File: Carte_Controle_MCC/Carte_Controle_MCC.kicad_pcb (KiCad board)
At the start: 2 copper layers, 35 parts, among them J1 USB_C_Receptacle_USB2.0_16P, J2 Conn_ST_STDC14, J3 Conn_01x02_XT60, J4 Conn_01x04_moteur, U1 USBLC6-2SC6, U2 STM32G431CBUx

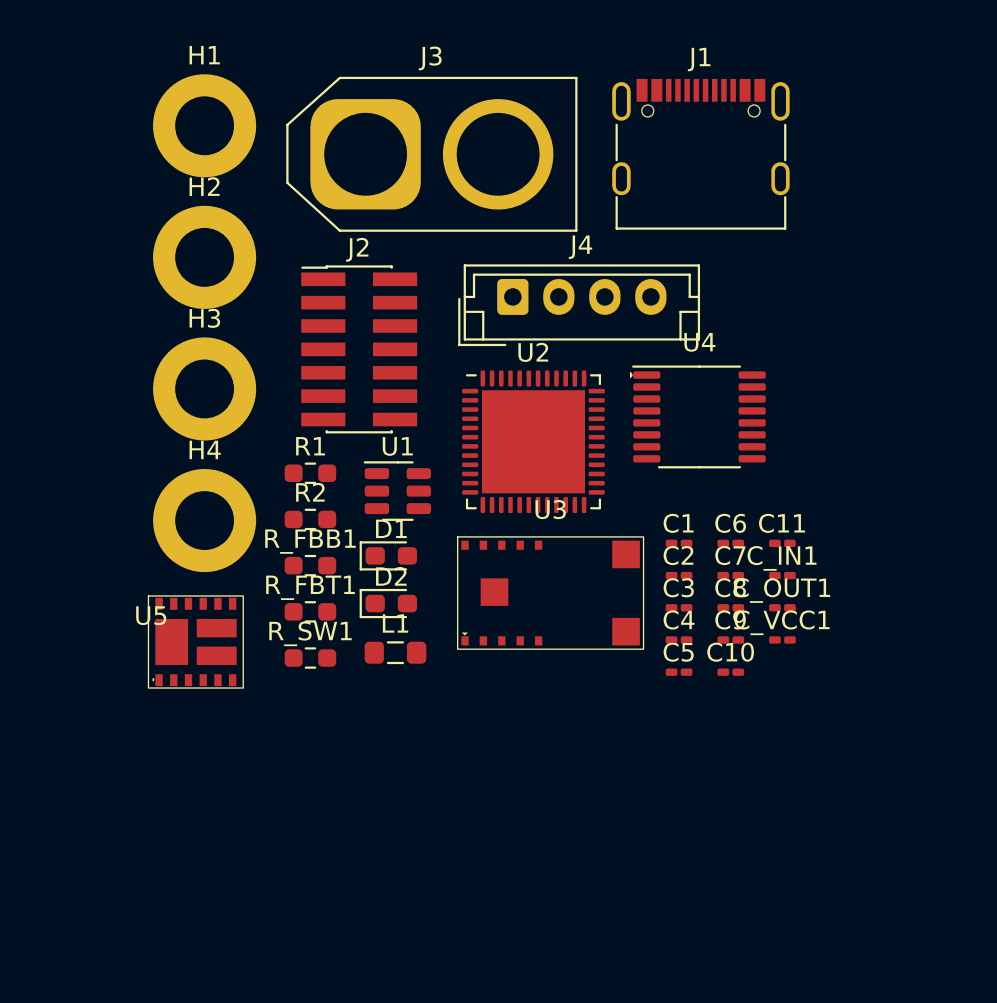
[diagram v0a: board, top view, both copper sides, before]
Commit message: routing of the PCB
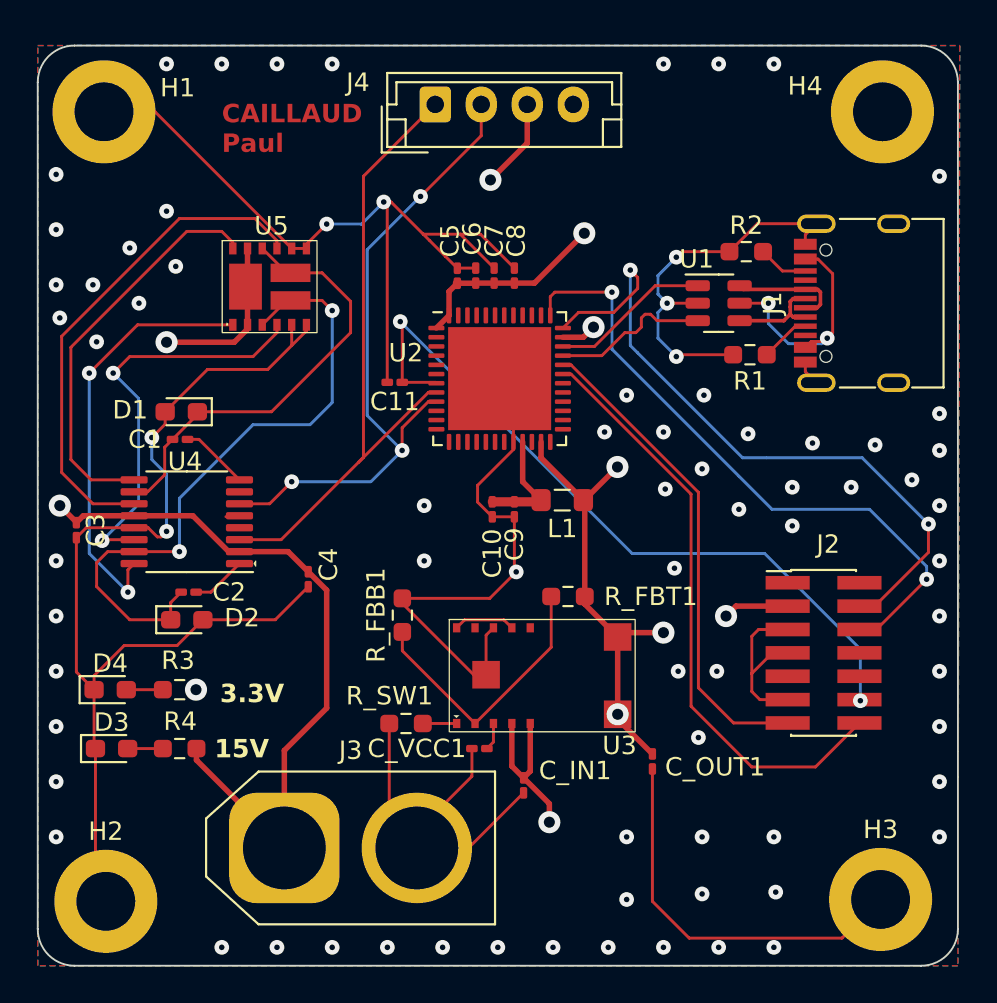
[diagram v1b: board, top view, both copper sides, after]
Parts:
- added D3: LED_Small, LED_SMD:LED_0603_1608Metric_Pad1.05x0.95mm_HandSolder, F.Cu at (114.0, 108.2)
- added D4: LED_Small, LED_SMD:LED_0603_1608Metric_Pad1.05x0.95mm_HandSolder, F.Cu at (113.9, 105.0)
- added R3: 820, Resistor_SMD:R_0603_1608Metric_Pad0.98x0.95mm_HandSolder, F.Cu at (117.7, 105.0)
- added R4: 5.6k, Resistor_SMD:R_0603_1608Metric_Pad0.98x0.95mm_HandSolder, F.Cu at (117.7, 108.2)
- moved H3 46.0 mm to (155.8, 116.4)
- moved H4 43.0 mm to (155.9, 73.6)
- moved J3 37.9 mm to (123.4, 113.6)
- moved H2 35.4 mm to (113.7, 116.5)
- moved C3 33.0 mm to (112.1, 96.3), turned to -90 degrees
- moved J2 30.1 mm to (152.7, 103.0)
- moved U4 28.4 mm to (118.1, 95.9), turned to 180 degrees
- moved R2 27.8 mm to (148.5, 81.2)
- moved C1 27.7 mm to (117.7, 91.4), turned to 180 degrees
- moved C2 26.7 mm to (118.2, 99.7)
- moved R1 24.7 mm to (148.7, 86.8), turned to 180 degrees
- moved C5 24.7 mm to (132.8, 82.5), turned to 90 degrees
- moved C11 22.8 mm to (129.4, 88.3), turned to 180 degrees
- moved C8 21.5 mm to (135.9, 82.5), turned to 90 degrees
- moved C7 20.8 mm to (134.8, 82.5), turned to 90 degrees
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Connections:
- J1 pad A1: ISO_GND -> GND
- J1 pad A12: ISO_GND -> GND
- J1 pad B1: ISO_GND -> GND
- J1 pad B12: ISO_GND -> GND
- J1 pad S1: ISO_GND -> GND
- R1 pad 2: ISO_GND -> GND
- R2 pad 1: ISO_GND -> GND
- U1 pad 2: ISO_GND -> GND
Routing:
- net GND: track 0.00 -> 209.6 mm, vias 0 -> 78
- net +15V: track 0.00 -> 63.1 mm, vias 0 -> 4
- net +3.3V: track 0.00 -> 41.1 mm, vias 0 -> 7
- net NRST: track 0.00 -> 40.5 mm, vias 0 -> 2
- net SYS_SWDIO: track 0.00 -> 36.9 mm, vias 0 -> 2
- net TIM2_CH2_PWM: track 0.00 -> 35.9 mm, vias 0 -> 3
- net S1/D2_INPUT: track 0.00 -> 35.5 mm, vias 0 -> 2
- net TIM2_CH1_PWM: track 0.00 -> 35.2 mm
- net SYS_SWCLK: track 0.00 -> 35.0 mm, vias 0 -> 2
- net USART_Tx: track 0.00 -> 32.7 mm
- net G3_INPUT: track 0.00 -> 27.3 mm
- net USART_Rx: track 0.00 -> 26.5 mm
- net S4/D3_INPUT: track 0.00 -> 24.0 mm
- net G1_INPUT: track 0.00 -> 23.3 mm, vias 0 -> 2
- net G2_INPUT: track 0.00 -> 22.5 mm, vias 0 -> 2
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- added copper zone on In2.Cu, net +15V
- added copper zone on In2.Cu, net +3.3V
- added copper zone on B.Cu, net GND
- added copper zone on F.Cu, net GND
- added copper zone on In1.Cu, net GND
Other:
- board outline added: 50 x 50 mm
- copper layers 2 -> 4
- board text added: "15V"
- board text added: "3.3V"
- board text added: "CAILLAUD Paul"

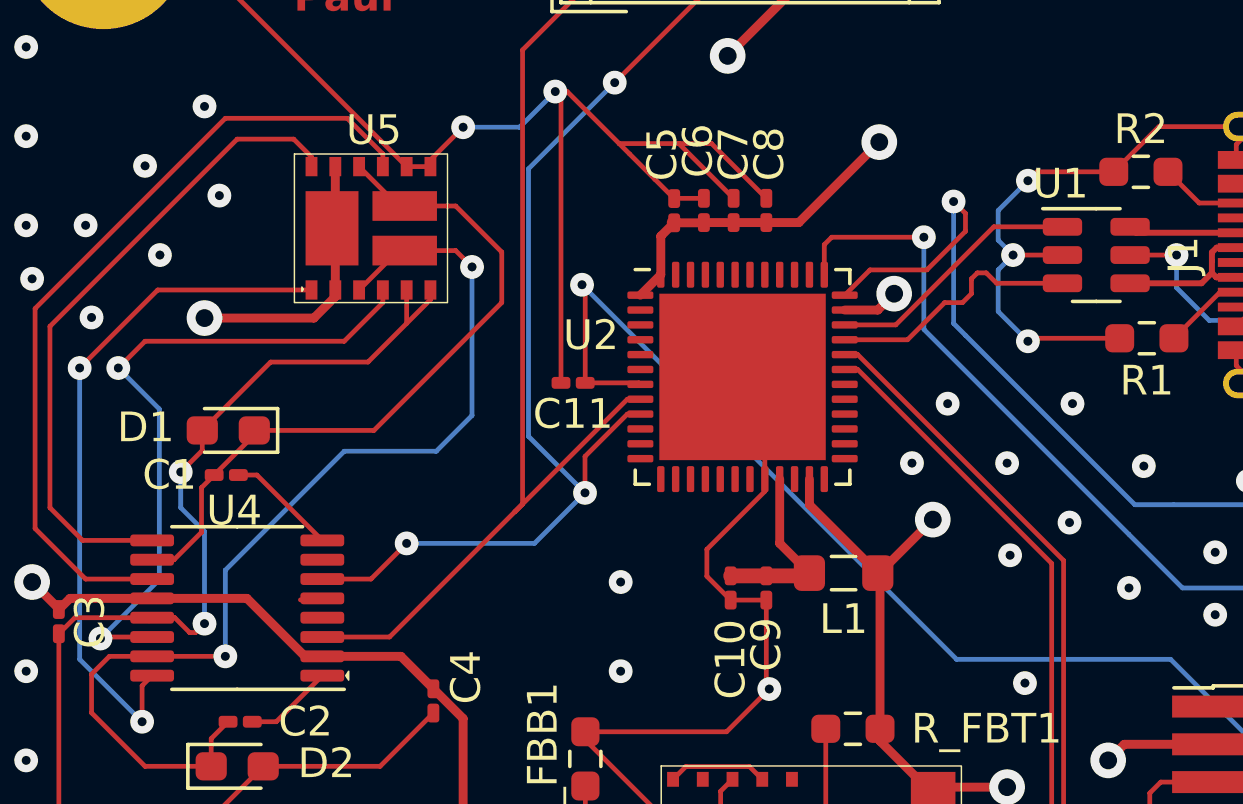
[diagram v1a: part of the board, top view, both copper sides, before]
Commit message: Suppression of unecessary ground tracks
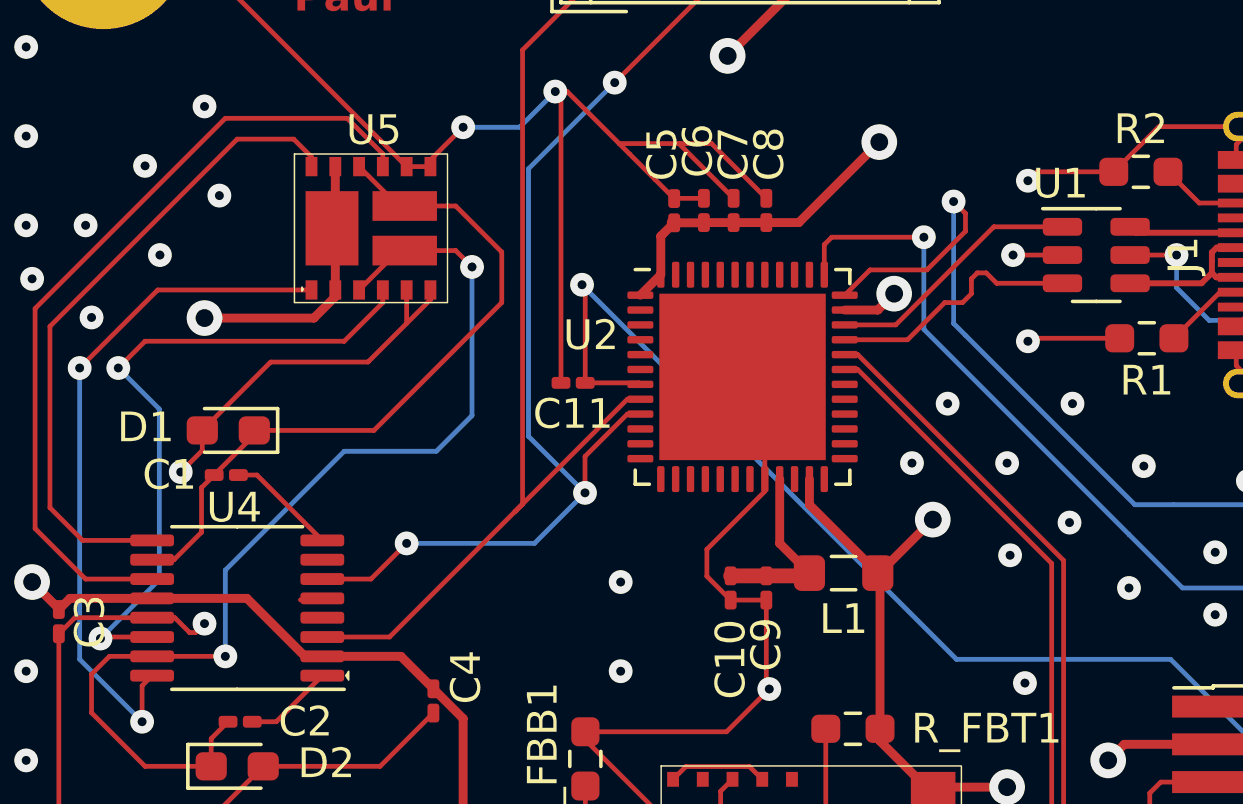
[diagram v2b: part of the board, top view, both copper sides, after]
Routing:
- net GND: track 209.6 -> 197.5 mm
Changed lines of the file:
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@@
     (property "Sheetname" "")
     (attr smd)
-    (fp_text reference "U4" (at 0.1 3.3 unlocked) (layer "F.SilkS")
+    (fp_text reference "U4" (at 0.1 3.4 unlocked) (layer "F.SilkS")
         (effects (font (size 1 1) (thickness 0.1)))
     )
@@
   (via (at 144.7 86.9) (size 0.8) (drill 0.3) (layers "F.Cu" "B.Cu") (net 6))
   (via (at 144 71) (size 0.8) (drill 0.3) (layers "F.Cu" "B.Cu") (free) (net 6))
-  (segment (start 143.7 84.5) (end 143.7 85.9) (width 0.16) (layer "B.Cu") (net 6))
-  (segment (start 117 93.3) (end 117 96.4) (width 0.16) (layer "B.Cu") (net 6))
   (segment (start 128.8 78.5) (end 127.6 79.7) (width 0.16) (layer "B.Cu") (net 6))
-  (segment (start 144.7 81.5) (end 143.7 82.5) (width 0.16) (layer "B.Cu") (net 6))
   (segment (start 127.6 79.7) (end 125.7 79.7) (width 0.16) (layer "B.Cu") (net 6))
-  (segment (start 116.2 91.3) (end 116.2 92.5) (width 0.16) (layer "B.Cu") (net 6))
-  (segment (start 116.8 93.1) (end 117 93.3) (width 0.16) (layer "B.Cu") (net 6))
-  (segment (start 143.7 85.9) (end 144.7 86.9) (width 0.16) (layer "B.Cu") (net 6))
-  (segment (start 143.7 83.5) (end 144.2 84) (width 0.16) (layer "B.Cu") (net 6))
-  (segment (start 116.2 92.5) (end 116.8 93.1) (width 0.16) (layer "B.Cu") (net 6))
-  (segment (start 143.7 82.5) (end 143.7 83.5) (width 0.16) (layer "B.Cu") (net 6))
-  (segment (start 144.2 84) (end 143.7 84.5) (width 0.16) (layer "B.Cu") (net 6))
   (segment (start 137 82.9) (end 139.7 80.2) (width 0.3) (layer "F.Cu") (net 7))
   (segment (start 132.35 84.6625) (end 132.35 83.365) (width 0.3) (layer "F.Cu") (net 7))
@@
   (segment (start 129.8125 101.8625) (end 129.8125 102.8875) (width 0.16) (layer "F.Cu") (net 29))
   (segment (start 130.925 106.8375) (end 132.7625 106.8375) (width 0.16) (layer "F.Cu") (net 30))
-  (segment (start 138.5375 86.35) (end 140.253087 86.35) (width 0.16) (layer "F.Cu") (net 31))
-  (segment (start 143.553087 83.05) (end 145.8625 83.05) (width 0.16) (layer "F.Cu") (net 31))
-  (segment (start 140.253087 86.35) (end 143.553087 83.05) (width 0.16) (layer "F.Cu") (net 31))
-  (segment (start 142.8 85.3) (end 142.8 84.8) (width 0.16) (layer "F.Cu") (net 32))
-  (segment (start 142.8 84.8) (end 143 84.6) (width 0.16) (layer "F.Cu") (net 32))
-  (segment (start 141.9 85.6) (end 142.5 85.6) (width 0.16) (layer "F.Cu") (net 32))
-  (segment (start 140.65 86.85) (end 141.9 85.6) (width 0.16) (layer "F.Cu") (net 32))
-  (segment (start 143 84.6) (end 143.3 84.6) (width 0.16) (layer "F.Cu") (net 32))
-  (segment (start 142.5 85.6) (end 142.8 85.3) (width 0.16) (layer "F.Cu") (net 32))
-  (segment (start 138.5375 86.85) (end 140.65 86.85) (width 0.16) (layer "F.Cu") (net 32))
-  (segment (start 143.65 84.95) (end 145.8625 84.95) (width 0.16) (layer "F.Cu") (net 32))
-  (segment (start 143.3 84.6) (end 143.65 84.95) (width 0.16) (layer "F.Cu") (net 32))
+  (segment (start 140.253087 86.35) (end 138.5375 86.35) (width 0.16) (layer "F.Cu") (net 31))
+  (segment (start 145.8625 83.05) (end 143.553087 83.05) (width 0.16) (layer "F.Cu") (net 31))
+  (segment (start 143.553087 83.05) (end 140.253087 86.35) (width 0.16) (layer "F.Cu") (net 31))
+  (segment (start 143 84.6) (end 142.8 84.8) (width 0.16) (layer "F.Cu") (net 32))
+  (segment (start 143.3 84.6) (end 143 84.6) (width 0.16) (layer "F.Cu") (net 32))
+  (segment (start 143.65 84.95) (end 143.3 84.6) (width 0.16) (layer "F.Cu") (net 32))
+  (segment (start 140.65 86.85) (end 138.5375 86.85) (width 0.16) (layer "F.Cu") (net 32))
+  (segment (start 142.5 85.6) (end 141.9 85.6) (width 0.16) (layer "F.Cu") (net 32))
+  (segment (start 142.8 85.3) (end 142.5 85.6) (width 0.16) (layer "F.Cu") (net 32))
+  (segment (start 141.9 85.6) (end 140.65 86.85) (width 0.16) (layer "F.Cu") (net 32))
+  (segment (start 142.8 84.8) (end 142.8 85.3) (width 0.16) (layer "F.Cu") (net 32))
+  (segment (start 145.8625 84.95) (end 143.65 84.95) (width 0.16) (layer "F.Cu") (net 32))
   (segment (start 135.3325 101.2075) (end 133.1925 101.2075) (width 0.16) (layer "F.Cu") (net 67))
   (segment (start 135.7625 101.6375) (end 135.3325 101.2075) (width 0.16) (layer "F.Cu") (net 67))
